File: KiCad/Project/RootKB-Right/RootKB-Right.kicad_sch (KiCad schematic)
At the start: 70 parts, among them J1 OLED-128x32, SW1 Switch, U1 Arduino_Pro_Micro, U2 TRRS

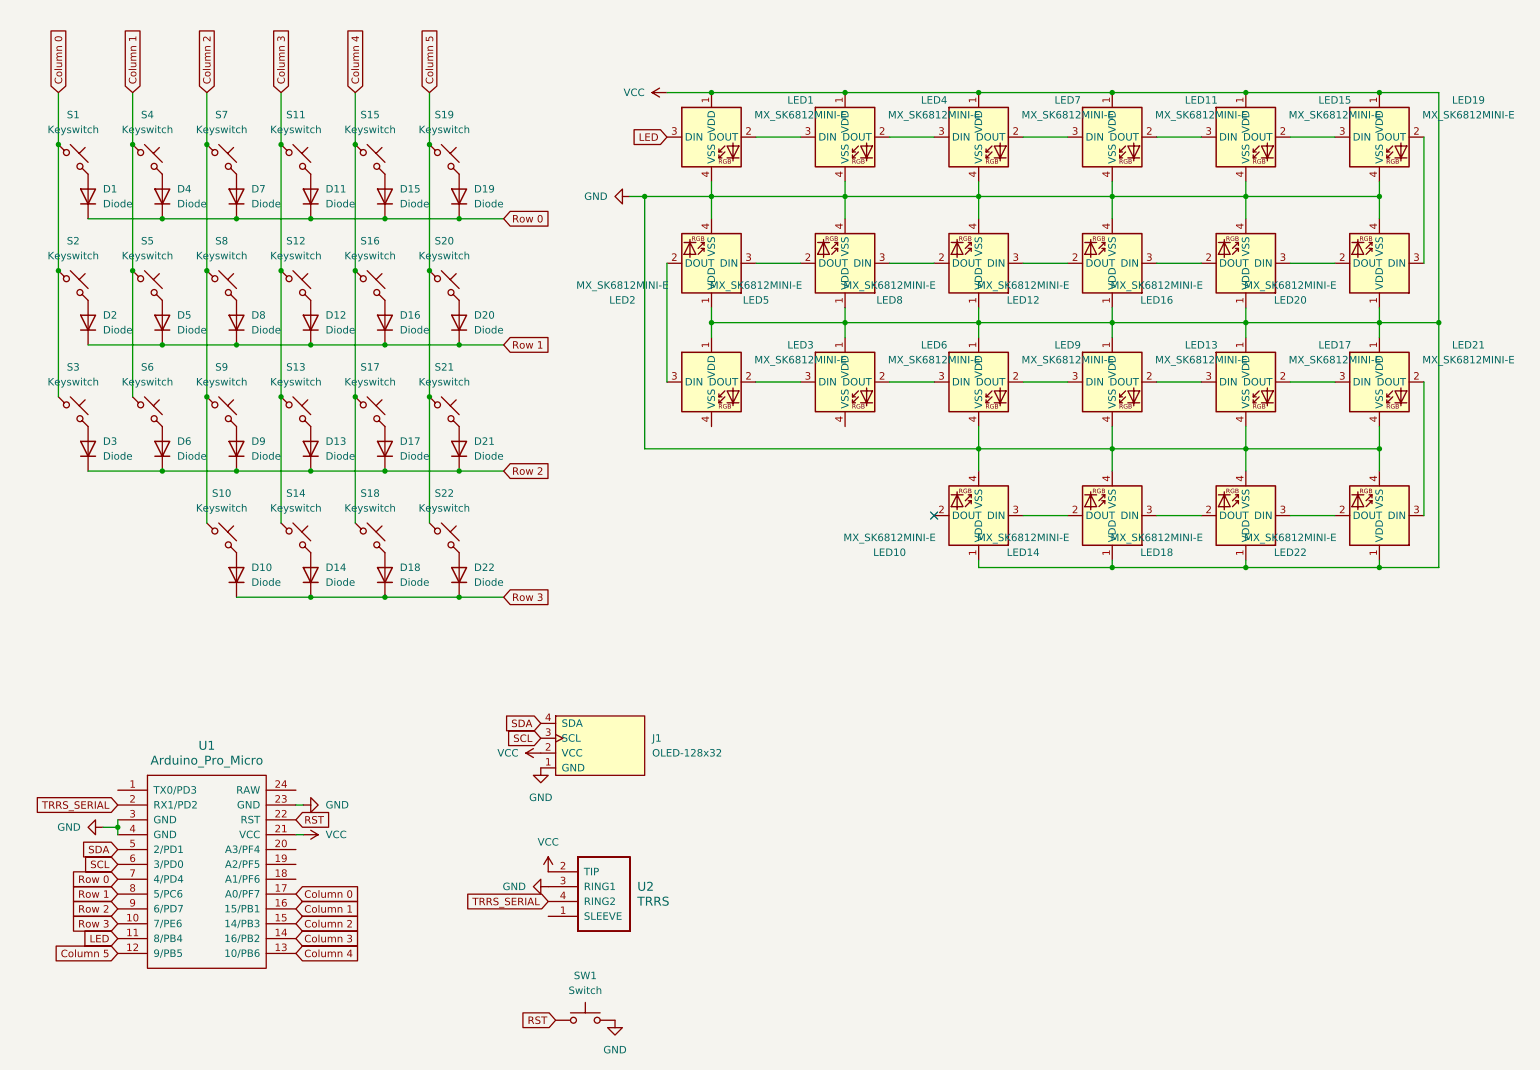
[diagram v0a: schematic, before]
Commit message: Make symmetrical right PCB
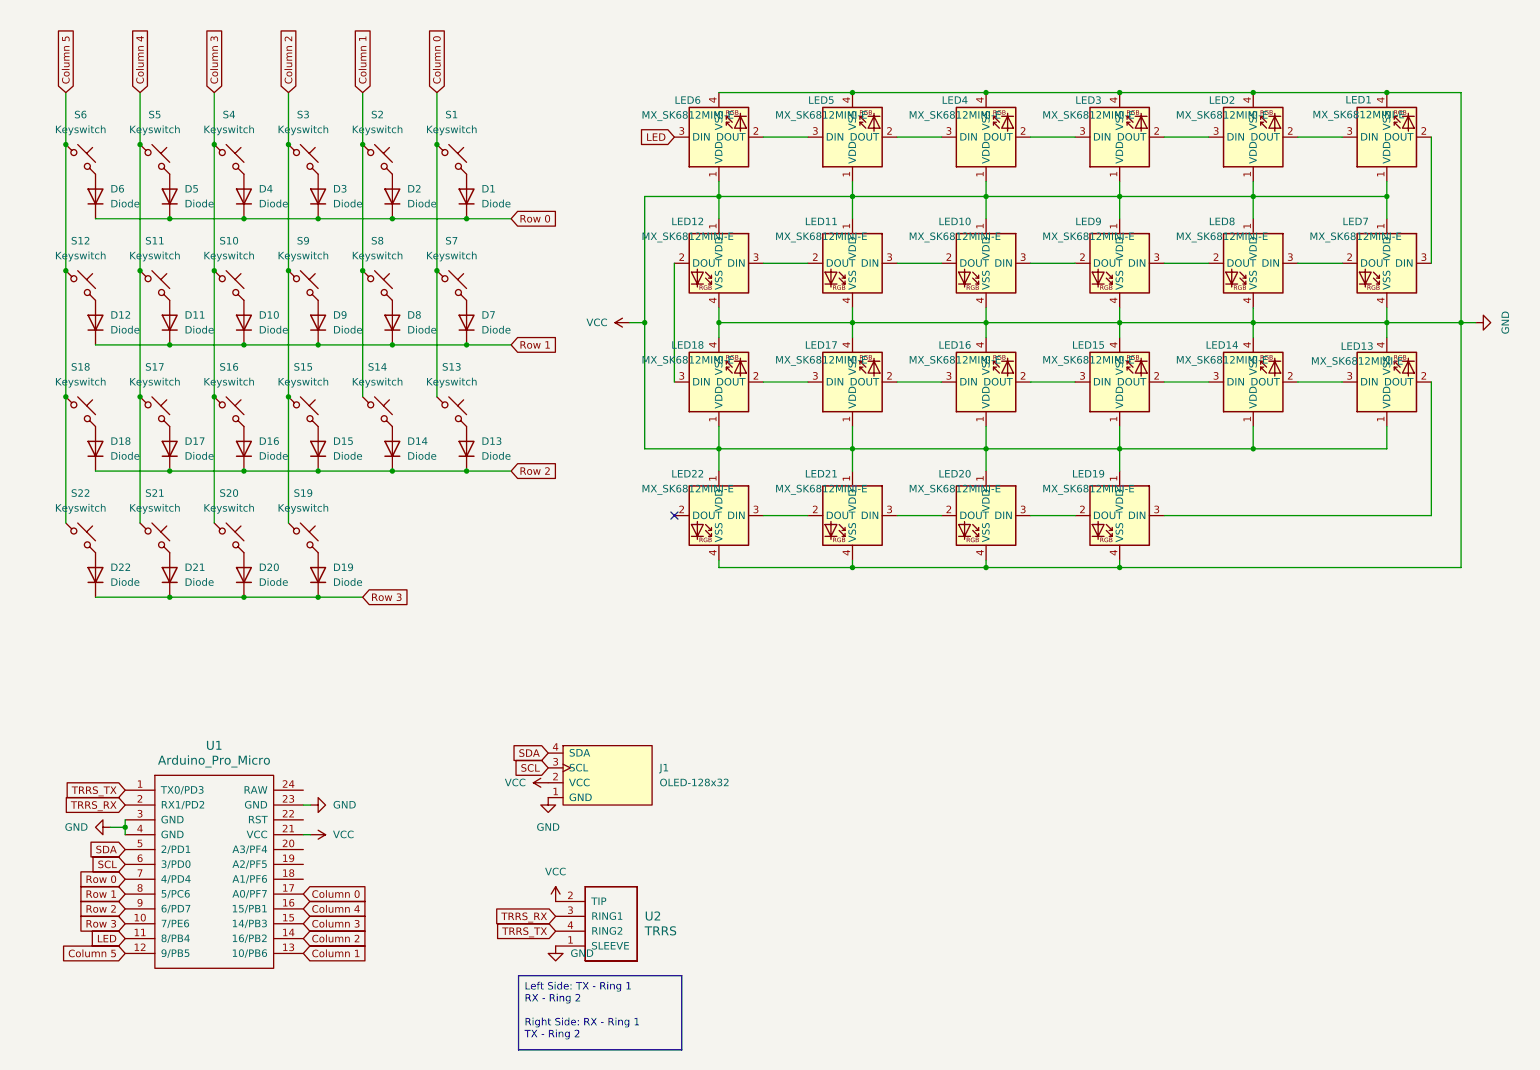
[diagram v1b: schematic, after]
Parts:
- removed SW1: Switch, ScottoKeebs_Components:Button_MJTP1250, symbol ScottoKeebs:Placeholder_Switch
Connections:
- net Column 0: now also S13.1, S7.1; no longer S2.1, S3.1
- net Column 1: now also S14.1, S2.1, S8.1, U1.13 (10/PB6); no longer S4.1, S5.1, S6.1, U1.16 (15/PB1)
- net Column 2: now also S15.1, S19.1, S3.1, U1.14 (16/PB2); no longer S10.1, S7.1, S8.1, U1.15 (14/PB3)
- net Column 3: now also S10.1, S16.1, S20.1, S4.1, U1.15 (14/PB3); no longer S11.1, S12.1, S13.1, S14.1, U1.14 (16/PB2)
- net Column 4: now also S11.1, S21.1, S5.1, U1.16 (15/PB1); no longer S15.1, S16.1, S18.1, U1.13 (10/PB6)
- net Column 5: now also S12.1, S18.1, S6.1; no longer S19.1, S20.1, S21.1
- net GND: now also LED3.4 (VSS), LED6.4 (VSS), U2.1 (SLEEVE); no longer U2.3 (RING1)
- net LED: now also LED6.3 (DIN); no longer LED1.3 (DIN)
- net Row 0: now also D2.1 (K), D3.1 (K), D5.1 (K), D6.1 (K); no longer D11.1 (K), D15.1 (K), D19.1 (K), D7.1 (K)
- net Row 1: now also D10.1 (K), D11.1 (K), D7.1 (K), D9.1 (K); no longer D16.1 (K), D2.1 (K), D20.1 (K), D5.1 (K)
- net Row 2: now also D14.1 (K), D15.1 (K), D16.1 (K), D18.1 (K); no longer D21.1 (K), D3.1 (K), D6.1 (K), D9.1 (K)
- net Row 3: now also D19.1 (K), D20.1 (K), D21.1 (K); no longer D10.1 (K), D14.1 (K), D18.1 (K)
- net at LED7.2 (DOUT): now also LED8.3 (DIN); no longer LED11.3 (DIN)
- net at LED7.3 (DIN): now also LED1.2 (DOUT); no longer LED4.2 (DOUT)
- net at LED10.3 (DIN): now also LED9.2 (DOUT); no longer LED14.2 (DOUT)
- net at LED18.2 (DOUT): now also LED17.3 (DIN); no longer LED14.3 (DIN)
- net at LED16.2 (DOUT): now also LED15.3 (DIN); no longer LED12.3 (DIN)
- net at LED20.2 (DOUT): now also LED21.3 (DIN); no longer LED16.3 (DIN)
- net at LED8.2 (DOUT): now also LED9.3 (DIN); no longer LED5.3 (DIN)
- net at LED12.2 (DOUT): now also LED18.3 (DIN); no longer LED8.3 (DIN)
- net at LED4.3 (DIN): now also LED5.2 (DOUT); no longer LED1.2 (DOUT)
- net at LED13.3 (DIN): now also LED14.2 (DOUT); no longer LED9.2 (DOUT)
- net at LED6.2 (DOUT): now also LED5.3 (DIN); no longer LED9.3 (DIN)
- net at LED3.2 (DOUT): now also LED2.3 (DIN); no longer LED6.3 (DIN)
- net at LED2.2 (DOUT): now also LED1.3 (DIN); no longer LED3.3 (DIN)
- net at LED11.2 (DOUT): now also LED12.3 (DIN); no longer LED15.3 (DIN)
- net at LED22.2 (DOUT): no longer LED18.3 (DIN)
- net at LED13.2 (DOUT): now also LED19.3 (DIN); no longer LED17.3 (DIN)
- net TRRS_TX: now reaches U1.1 (TX0/PD3)
- net TRRS_TX: now also U2.4 (RING2)
- net at LED17.2 (DOUT): now also LED16.3 (DIN); no longer LED21.3 (DIN)
- net at LED15.2 (DOUT): now also LED14.3 (DIN); no longer LED19.3 (DIN)
- net at LED10.2 (DOUT): now also LED11.3 (DIN)
- net RST: no longer names the net of U1.22 (RST)
- net TRRS_SERIAL renamed TRRS_RX
- net TRRS_RX: now also U2.3 (RING1); no longer U2.4 (RING2)
- new net: LED3.3 (DIN), LED4.2 (DOUT)

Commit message: add titles
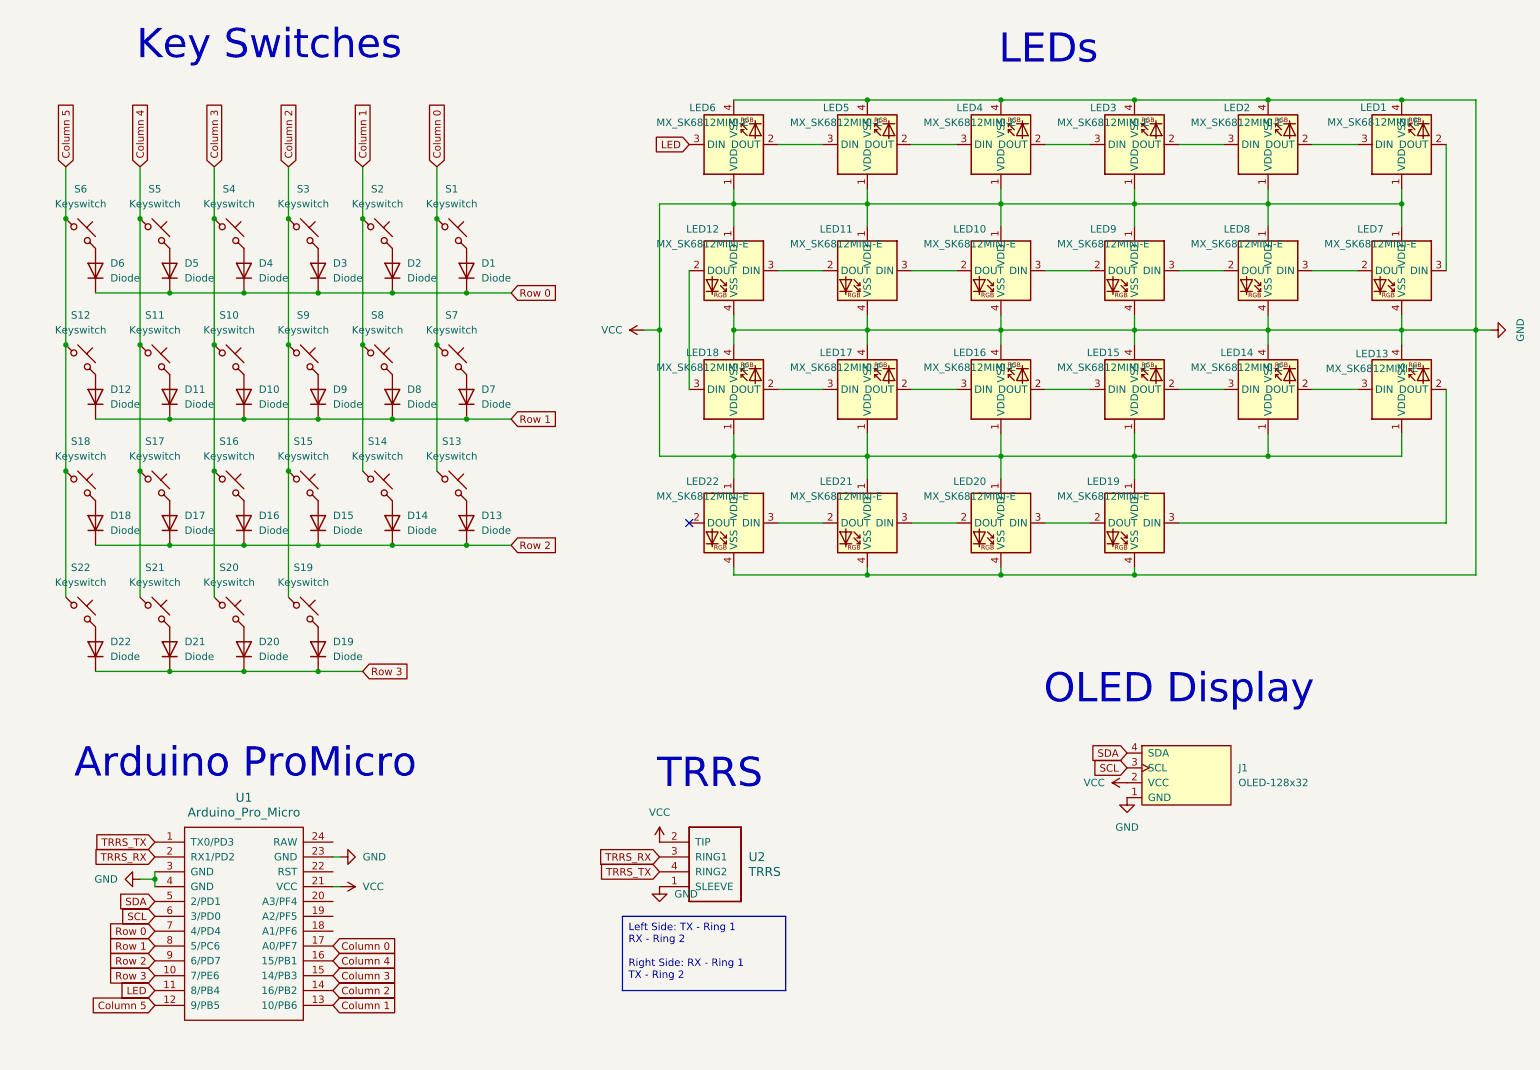
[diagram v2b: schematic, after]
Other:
- note added: "Arduino ProMicro"
- note added: "Key Switches"
- note added: "LEDs"
- note added: "OLED Display"
- note added: "TRRS"
- title: RootKB -> RootKB-Right
- moved on the sheet: D1, D10, D11, D12, D13, D14, D15, D16, D17, D18, D19, D2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

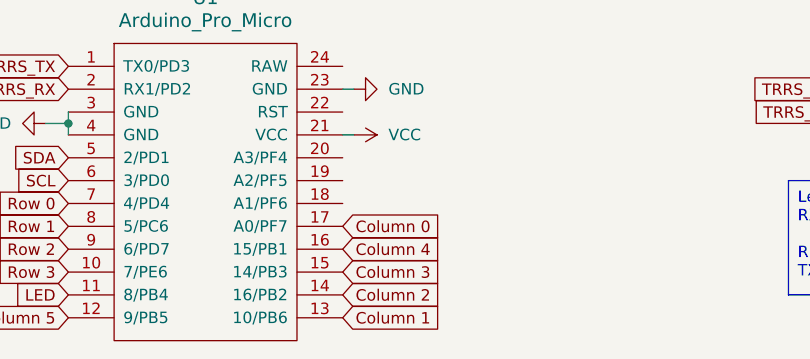
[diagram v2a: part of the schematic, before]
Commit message: route tracks on right side
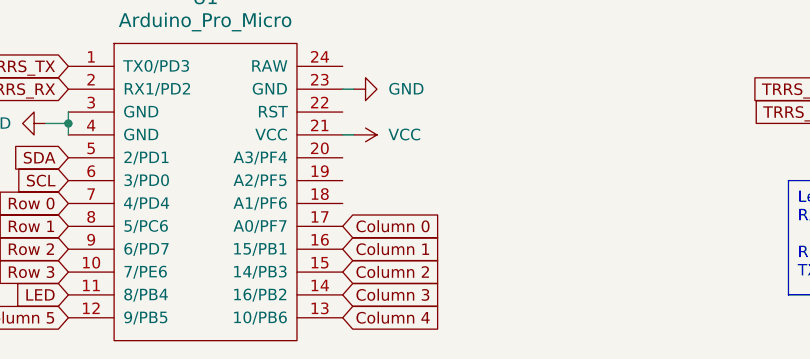
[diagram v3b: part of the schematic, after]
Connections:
- net Column 1: now also U1.16 (15/PB1); no longer U1.13 (10/PB6)
- net Column 2: now also U1.15 (14/PB3); no longer U1.14 (16/PB2)
- net Column 3: now also U1.14 (16/PB2); no longer U1.15 (14/PB3)
- net Column 4: now also U1.13 (10/PB6); no longer U1.16 (15/PB1)
